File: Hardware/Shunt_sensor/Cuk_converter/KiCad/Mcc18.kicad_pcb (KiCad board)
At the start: 2 copper layers, 199.1 x 107.2 mm, 62 parts, among them Q1 IRFP4321PbF, U1 INA240, U2 DRIVER_(INEP), U3 LM7812_TO220, U4 Signals_MCC, U5 ZCS, U6 INA211

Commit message: fixed and created all Fabrication files
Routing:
- added copper zone on B.Cu, net (none)
- added copper zone on F.Cu, net (none)
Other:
- board size 199.1 x 107.2 mm -> 199.1 x 118.4 mm
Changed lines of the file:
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@@
   (general
     (thickness 1.6)
-    (drawings 8)
+    (drawings 13)
     (tracks 671)
     (zones 0)
@@
     (pad_drill 2.2)
     (pad_to_mask_clearance 0.2)
-    (aux_axis_origin 50.038 39.878)
+    (aux_axis_origin 50.038 34.29)
+    (grid_origin 50.038 34.29)
     (visible_elements 7FFFFFFF)
     (pcbplotparams
@@
       (padsonsilk false)
       (subtractmaskfromsilk true)
-      (outputformat 4)
+      (outputformat 1)
       (mirror false)
       (drillshape 0)
@@
     )
   )
-  (gr_line (start 50.038 147.066) (end 50.038 39.878) (layer Edge.Cuts) (width 0.15))
-  (gr_line (start 249.174 147.066) (end 50.038 147.066) (layer Edge.Cuts) (width 0.15))
-  (gr_line (start 249.174 39.878) (end 249.174 147.066) (layer Edge.Cuts) (width 0.15))
-  (gr_line (start 50.038 39.878) (end 249.174 39.878) (layer Edge.Cuts) (width 0.15))
-  (dimension 202.184 (width 0.3) (layer Dwgs.User)
-    (gr_text "7.9600 in" (at 151.13 155.262) (layer Dwgs.User)
+  (dimension 199.136 (width 0.3) (layer Dwgs.User)
+    (gr_text "7,8400 em" (at 149.606 161.358) (layer Dwgs.User)
       (effects (font (size 1.5 1.5) (thickness 0.3)))
     )
-    (feature1 (pts (xy 252.222 147.066) (xy 252.222 153.748421)))
-    (feature2 (pts (xy 50.038 147.066) (xy 50.038 153.748421)))
-    (crossbar (pts (xy 50.038 153.162) (xy 252.222 153.162)))
-    (arrow1a (pts (xy 252.222 153.162) (xy 251.095496 153.748421)))
-    (arrow1b (pts (xy 252.222 153.162) (xy 251.095496 152.575579)))
-    (arrow2a (pts (xy 50.038 153.162) (xy 51.164504 153.748421)))
-    (arrow2b (pts (xy 50.038 153.162) (xy 51.164504 152.575579)))
+    (feature1 (pts (xy 249.174 152.654) (xy 249.174 159.844421)))
+    (feature2 (pts (xy 50.038 152.654) (xy 50.038 159.844421)))
+    (crossbar (pts (xy 50.038 159.258) (xy 249.174 159.258)))
+    (arrow1a (pts (xy 249.174 159.258) (xy 248.047496 159.844421)))
+    (arrow1b (pts (xy 249.174 159.258) (xy 248.047496 158.671579)))
+    (arrow2a (pts (xy 50.038 159.258) (xy 51.164504 159.844421)))
+    (arrow2b (pts (xy 50.038 159.258) (xy 51.164504 158.671579)))
   )
-  (dimension 202.18416 (width 0.3) (layer Dwgs.User)
-    (gr_text "202.184 mm" (at 151.148273 161.738339 0.07197958464) (layer Dwgs.User)
+  (dimension 199.136 (width 0.3) (layer Dwgs.User)
+    (gr_text "199,136 mm" (at 149.606 157.802) (layer Dwgs.User)
       (effects (font (size 1.5 1.5) (thickness 0.3)))
     )
-    (feature1 (pts (xy 50.038 147.32) (xy 50.054372 160.351761)))
-    (feature2 (pts (xy 252.222 147.066) (xy 252.238372 160.097761)))
-    (crossbar (pts (xy 252.237635 159.511341) (xy 50.053635 159.765341)))
-    (arrow1a (pts (xy 50.053635 159.765341) (xy 51.179401 159.177506)))
-    (arrow1b (pts (xy 50.053635 159.765341) (xy 51.180875 160.350346)))
-    (arrow2a (pts (xy 252.237635 159.511341) (xy 251.110395 158.926336)))
-    (arrow2b (pts (xy 252.237635 159.511341) (xy 251.111869 160.099176)))
+    (feature1 (pts (xy 249.174 152.654) (xy 249.174 156.288421)))
+    (feature2 (pts (xy 50.038 152.654) (xy 50.038 156.288421)))
+    (crossbar (pts (xy 50.038 155.702) (xy 249.174 155.702)))
+    (arrow1a (pts (xy 249.174 155.702) (xy 248.047496 156.288421)))
+    (arrow1b (pts (xy 249.174 155.702) (xy 248.047496 155.115579)))
+    (arrow2a (pts (xy 50.038 155.702) (xy 51.164504 156.288421)))
+    (arrow2b (pts (xy 50.038 155.702) (xy 51.164504 155.115579)))
   )
-  (dimension 107.188301 (width 0.3) (layer Dwgs.User)
-    (gr_text "4.2200 in" (at 41.211258 93.493217 270.1357717) (layer Dwgs.User)
+  (dimension 118.364 (width 0.3) (layer Dwgs.User)
+    (gr_text "118,364 mm" (at 44.636 93.472 270) (layer Dwgs.User)
       (effects (font (size 1.5 1.5) (thickness 0.3)))
     )
-    (feature1 (pts (xy 50.292 147.066) (xy 42.851833 147.083631)))
-    (feature2 (pts (xy 50.038 39.878) (xy 42.597833 39.895631)))
-    (crossbar (pts (xy 43.184252 39.894241) (xy 43.438252 147.082241)))
-    (arrow1a (pts (xy 43.438252 147.082241) (xy 42.849163 145.95713)))
-    (arrow1b (pts (xy 43.438252 147.082241) (xy 44.022002 145.954351)))
-    (arrow2a (pts (xy 43.184252 39.894241) (xy 42.600502 41.022131)))
-    (arrow2b (pts (xy 43.184252 39.894241) (xy 43.773341 41.019352)))
-  )
-  (dimension 107.188 (width 0.3) (layer Dwgs.User)
-    (gr_text "107.188 mm" (at 36.508 93.472 270) (layer Dwgs.User)
+    (feature1 (pts (xy 50.038 152.654) (xy 46.149579 152.654)))
+    (feature2 (pts (xy 50.038 34.29) (xy 46.149579 34.29)))
+    (crossbar (pts (xy 46.736 34.29) (xy 46.736 152.654)))
+    (arrow1a (pts (xy 46.736 152.654) (xy 46.149579 151.527496)))
+    (arrow1b (pts (xy 46.736 152.654) (xy 47.322421 151.527496)))
+    (arrow2a (pts (xy 46.736 34.29) (xy 46.149579 35.416504)))
+    (arrow2b (pts (xy 46.736 34.29) (xy 47.322421 35.416504)))
+  )
+  (target plus (at 50.038 34.29) (size 5) (width 0.15) (layer Edge.Cuts))
+  (gr_line (start 50.038 39.878) (end 50.038 34.29) (layer Edge.Cuts) (width 0.15))
+  (gr_line (start 249.174 34.29) (end 249.174 39.878) (layer Edge.Cuts) (width 0.15))
+  (gr_line (start 249.174 152.654) (end 249.174 147.066) (layer Edge.Cuts) (width 0.15))
+  (gr_line (start 50.038 147.066) (end 50.038 152.654) (layer Edge.Cuts) (width 0.15))
+  (gr_line (start 50.038 147.066) (end 50.038 39.878) (layer Edge.Cuts) (width 0.15))
+  (gr_line (start 249.174 152.654) (end 50.038 152.654) (layer Edge.Cuts) (width 0.15))
+  (gr_line (start 249.174 39.878) (end 249.174 147.066) (layer Edge.Cuts) (width 0.15))
+  (gr_line (start 50.038 34.29) (end 249.174 34.29) (layer Edge.Cuts) (width 0.15))
+  (dimension 118.364 (width 0.3) (layer Dwgs.User)
+    (gr_text "4,6600 em" (at 41.084233 93.472 270) (layer Dwgs.User)
       (effects (font (size 1.5 1.5) (thickness 0.3)))
     )
-    (feature1 (pts (xy 50.038 147.066) (xy 38.021579 147.066)))
-    (feature2 (pts (xy 50.038 39.878) (xy 38.021579 39.878)))
-    (crossbar (pts (xy 38.608 39.878) (xy 38.608 147.066)))
-    (arrow1a (pts (xy 38.608 147.066) (xy 38.021579 145.939496)))
-    (arrow1b (pts (xy 38.608 147.066) (xy 39.194421 145.939496)))
-    (arrow2a (pts (xy 38.608 39.878) (xy 38.021579 41.004504)))
-    (arrow2b (pts (xy 38.608 39.878) (xy 39.194421 41.004504)))
+    (feature1 (pts (xy 50.038 152.654) (xy 42.597812 152.654)))
+    (feature2 (pts (xy 50.038 34.29) (xy 42.597812 34.29)))
+    (crossbar (pts (xy 43.184233 34.29) (xy 43.184233 152.654)))
+    (arrow1a (pts (xy 43.184233 152.654) (xy 42.597812 151.527496)))
+    (arrow1b (pts (xy 43.184233 152.654) (xy 43.770654 151.527496)))
+    (arrow2a (pts (xy 43.184233 34.29) (xy 42.597812 35.416504)))
+    (arrow2b (pts (xy 43.184233 34.29) (xy 43.770654 35.416504)))
   )
   (segment (start 102.616 60.5005) (end 102.616 58.1175) (width 1) (layer F.Cu) (net 1) (status 30))
@@
   )
   (zone (net 38) (net_name GND) (layer B.Cu) (hatch edge 0.508)
+    (priority 1)
     (connect_pads yes (clearance 0.3048))
     (min_thickness 0.508)
@@
   )
   (zone (net 45) (net_name /+B) (layer F.Cu) (hatch edge 0.508)
+    (priority 1)
     (connect_pads yes (clearance 1.27))
     (min_thickness 0.508)
@@
       )
     )
+  )
+  (zone (net 0) (net_name "") (layer F.Cu) (hatch edge 0.508)
+    (connect_pads yes (clearance 1.27))
+    (min_thickness 0.508)
+    (fill yes (arc_segments 16) (thermal_gap 0.508) (thermal_bridge_width 0.508))
+    (polygon
+      (pts
+        (xy 249.174 147.066) (xy 249.174 152.654) (xy 50.038 152.654) (xy 50.038 147.066)
+      )
+    )
+  )
+  (zone (net 0) (net_name "") (layer B.Cu) (hatch edge 0.508)
+    (connect_pads yes (clearance 1.27))
+    (min_thickness 0.508)
+    (fill yes (arc_segments 16) (thermal_gap 0.508) (thermal_bridge_width 0.508))
+    (polygon
+      (pts
+        (xy 249.174 147.066) (xy 249.174 152.654) (xy 50.038 152.654) (xy 50.038 147.066)
+      )
+    )
+  )
+  (zone (net 0) (net_name "") (layer B.Cu) (hatch edge 0.508)
+    (connect_pads yes (clearance 1.27))
+    (min_thickness 0.508)
+    (fill yes (arc_segments 16) (thermal_gap 0.508) (thermal_bridge_width 0.508) (smoothing chamfer) (radius 4))
+    (polygon
+      (pts
+        (xy 50.038 34.29) (xy 249.174 34.29) (xy 249.174 39.878) (xy 50.038 39.878)
+      )
+    )
+  )
+  (zone (net 0) (net_name "") (layer F.Cu) (hatch edge 0.508)
+    (connect_pads yes (clearance 1.27))
+    (min_thickness 0.508)
+    (fill yes (arc_segments 16) (thermal_gap 0.508) (thermal_bridge_width 0.508) (smoothing chamfer) (radius 4))
+    (polygon
+      (pts
+        (xy 50.038 34.29) (xy 249.174 34.29) (xy 249.174 39.878) (xy 50.038 39.878)
+      )
+    )

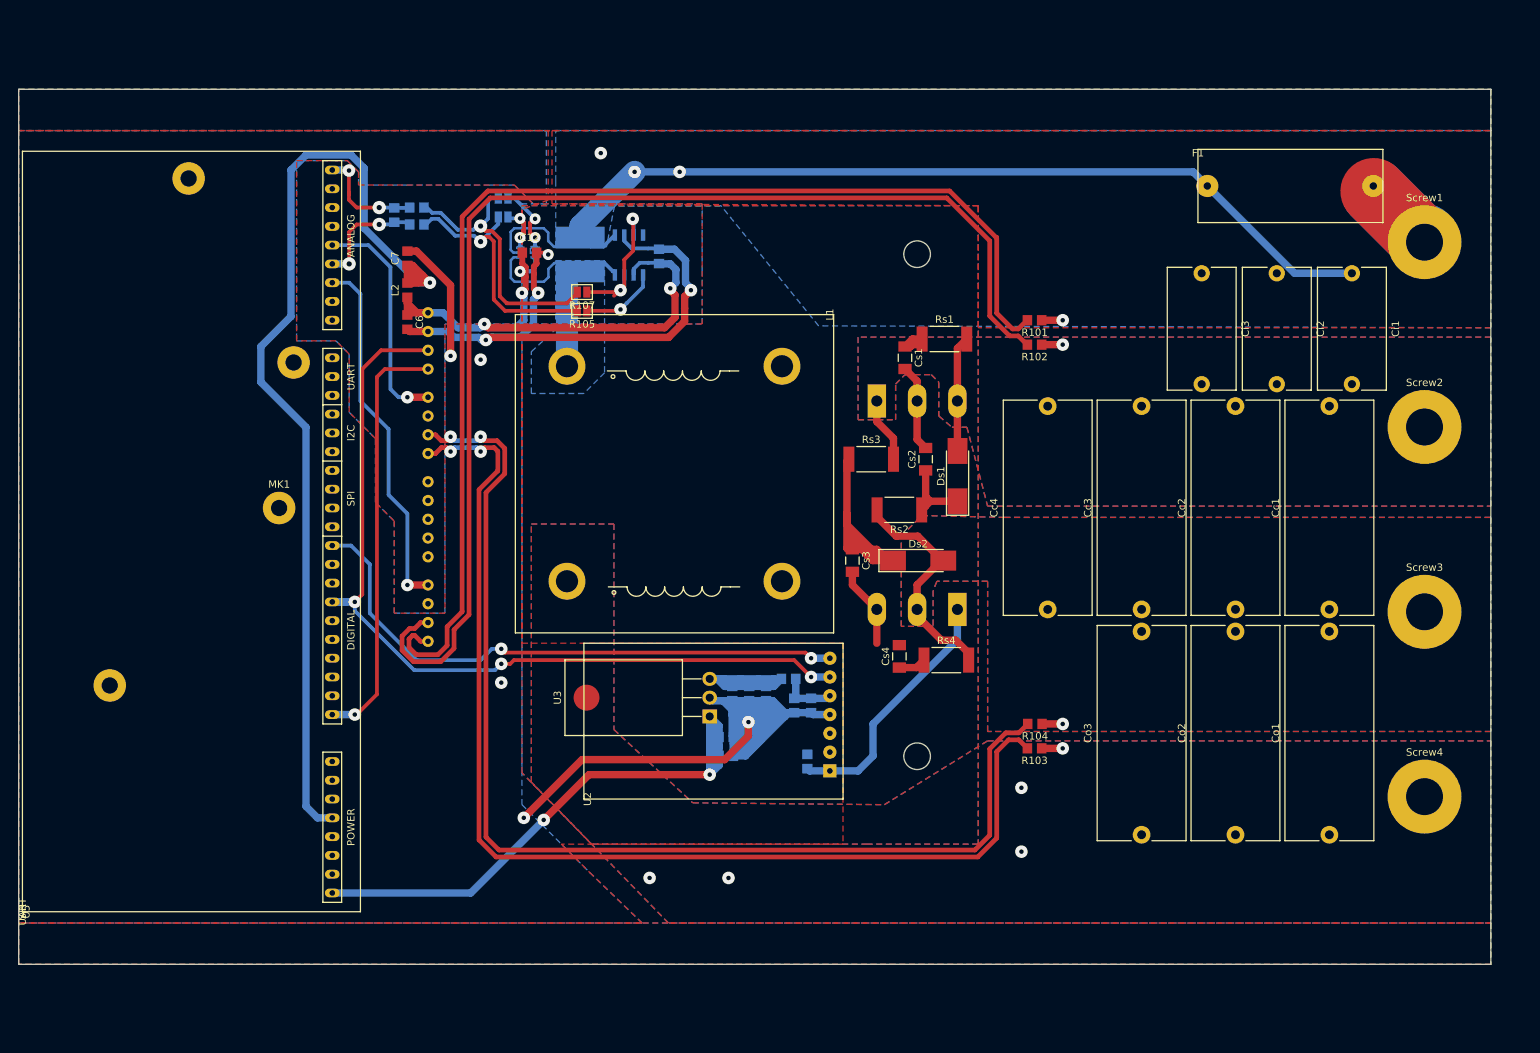
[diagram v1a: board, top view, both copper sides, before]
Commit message: Shunt_Cuk fixed _Switchs of the cuk fixed_ _Added isolation between the high voltage and the low voltage_
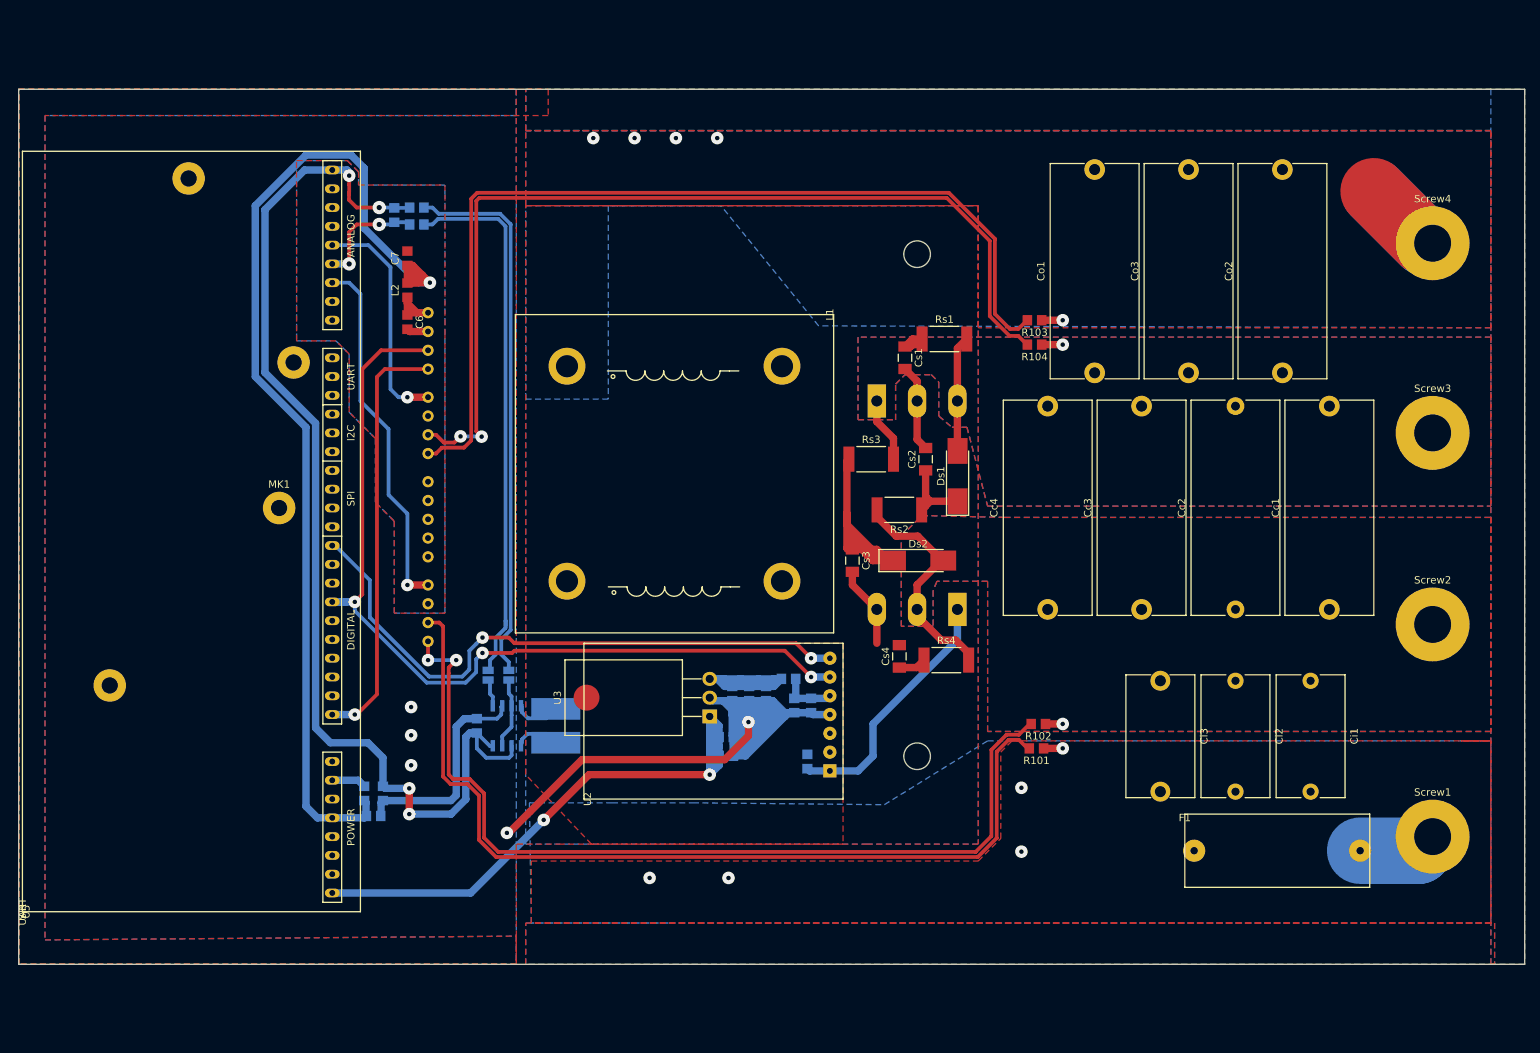
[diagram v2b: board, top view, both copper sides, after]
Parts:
- removed R106, R108: 0R, Jumper:SolderJumper-2_P1.3mm_Open_Pad1.0x1.5mm
- removed U6: INA211, MCCplaca Shunt:INA211BIDCKR
- added C13: 100nF, MCC:C_0805_2012Metric_Pad1.29x1.40mm_HandSolder, B.Cu at (96.8, 129.5)
- added L4: L_Small, Inductor_SMD:L_0805_2012Metric_Pad1.29x1.40mm_HandSolder, B.Cu at (98.0, 132.6)
- C12: footprint MCCplaca Shunt:C_0805_2012Metric_Pad1.29x1.40mm_HandSolder -> MCC:C_0805_2012Metric_Pad1.29x1.40mm_HandSolder; moved to B.Cu
- R105, R107: moved to B.Cu
- U4: footprint MCCplaca Shunt:Signals -> MCCplaca:Signals
- moved F1 89.9 mm to (207.8, 132.3)
- moved Screw1 80.4 mm to (241.3, 135.4)
- moved C12 75.8 mm to (99.3, 129.5), turned to 90 degrees
- moved Screw4 74.9 mm to (241.3, 55.1)
- moved Co1 70.1 mm to (195.6, 72.6)
- moved C11 68.1 mm to (112.0, 120.4), turned to 90 degrees
- moved U1 65.8 mm to (116.1, 120.4), turned to 90 degrees
- moved Rshunt1 63.8 mm to (122.7, 120.4), turned to 270 degrees
- moved Co2 62.8 mm to (221.0, 72.6)
- moved Co3 62.8 mm to (208.3, 72.6)
- moved R101 57.9 mm to (187.7, 123.4)
- moved R103 57.9 mm to (187.5, 65.5)
- moved Ci1 55.4 mm to (224.8, 114.3)
- moved Ci2 55.4 mm to (214.6, 114.3)
- moved Ci3 55.4 mm to (204.5, 114.3)
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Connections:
- C12 pad 1: GNDA -> +5VA
- C12 pad 2: +5VA -> GNDA
- Cc1 pad 1: /-B -> /+Vp
- Cc1 pad 2: /+Vp -> /-B
- Cc2 pad 1: /-B -> /+Vp
- Cc2 pad 2: /+Vp -> /-B
- Cc3 pad 1: /-B -> /+Vp
- Cc3 pad 2: /+Vp -> /-B
- Cc4 pad 1: /-B -> /+Vp
- Cc4 pad 2: /+Vp -> /-B
- Ci1 pad 1: /-Vp -> /+Vp
- Ci1 pad 2: /+Vp -> /-Vp
- Ci2 pad 1: /-Vp -> /+Vp
- Ci2 pad 2: /+Vp -> /-Vp
- Ci3 pad 1: /-Vp -> /+Vp
- Ci3 pad 2: /+Vp -> /-Vp
- Co1 pad 1: /+B -> /-B
- Co1 pad 2: /-B -> /+B
- Co2 pad 1: /+B -> /-B
- Co2 pad 2: /-B -> /+B
- Co3 pad 1: /+B -> /-B
- Co3 pad 2: /-B -> /+B
- D1 pad 1: /+Vp -> /-B
- D1 pad 3: /+Vp -> /-B
- Ds1 pad 2: /+Vp -> /-B
- Ds2 pad 2: /-B -> /+Vp
- L1 pad 1: /Rs+ -> /+B
- L1 pad 3: /+B -> /Rs+
- Q1 pad 2: /-B -> /+Vp
- Rs1 pad 2: /+Vp -> /-B
- Rs2 pad 2: /-B -> /+Vp
- Rs3 pad 2: /+Vp -> /-B
- Rs4 pad 2: /-B -> /+Vp
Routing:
- net /-Vp: track 146.4 -> 8.22 mm, vias 4 -> 5
- net +5VA: track 80.5 -> 37.6 mm, vias 4 -> 0
- net /Vp_sen+: track 164.5 -> 123.5 mm
- net /Vp_sen-: track 161.7 -> 123.7 mm, vias 0 -> 2
- net /Ip_sen+: track 36.0 -> 73.4 mm, vias 1 -> 0
- net /Ip_sen-: track 37.8 -> 74.0 mm, vias 1 -> 0
- net /Rs+: track 37.4 -> 6.39 mm
- net GNDA: track 133.4 -> 163.7 mm, vias 10 -> 4
- net /Vb_sen+: track 153.5 -> 128.9 mm, vias 2 -> 0
- net GND: track 251.0 -> 226.5 mm
- net /Vb_sen-: track 153.6 -> 130.0 mm
- net /+B: track 2.36 -> 22.5 mm
- net /INA211_OUT: track 11.7 -> 0.00 mm, vias 2 -> 0
- net /-P_unfused: track 19.8 -> 10.6 mm
- net +5V: track 139.7 -> 147.3 mm
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- removed copper zone on B.Cu, net /Rs+
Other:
- board size 199.1 x 118.4 mm -> 203.7 x 118.4 mm

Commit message: Fixed errors
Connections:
- C11 pad 2: +5VA -> Net-(C11-Pad2)
- C12 pad 1: +5VA -> Net-(C11-Pad2)
- L4 pad 1: +5VA -> Net-(C11-Pad2)
- U1 pad 6: +5VA -> Net-(C11-Pad2)
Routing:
- net Net-(C11-Pad2): track 0.00 -> 29.7 mm
- net +5VA: track 37.6 -> 7.91 mm
- net GND: track 226.5 -> 241.8 mm
- net /Source: track 23.8 -> 35.7 mm
- net /Vp_sen-: track 123.7 -> 121.5 mm, vias 2 -> 0
- net /Vb_sen-: track 130.0 -> 128.3 mm
- net /Vp_sen+: track 123.5 -> 121.9 mm
- net GNDA: track 163.7 -> 164.9 mm
- net /Gate: track 40.7 -> 39.6 mm
- net /Ip_sen-: track 74.0 -> 73.3 mm
- net /Ip_sen+: track 73.4 -> 72.7 mm
- added copper zone on B.Cu, net /Rs+
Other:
- board size 203.7 x 118.4 mm -> 199.2 x 138.3 mm
- rule trace_min: 0.3429 -> 0.0508
